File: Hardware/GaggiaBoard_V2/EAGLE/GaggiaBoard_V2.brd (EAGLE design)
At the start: 102 x 92 mm, 115 parts, among them IC1 LD117AS33TR, J1 4PIN, J11 PIN262409-1, J12 PIN262409-1, J13 PIN262409-1, J14 PIN262409-1, J15 PIN262409-1, J16 PIN262409-1, J17 PIN262409-1, J18 PIN262409-1, J19 PIN262409-1, J2 Vertical Qwiic Connector, J20 PIN262409-1, J3 Vertical Qwiic Connector, J5 2PIN, J6 3PIN, J7 3PIN, J8 5PIN, J9 3PIN, K1 RELAY-SPDT-JZC-11F, K2 RELAY-SPDT-JZC-11F, K3 AQH213, Q1 600mA/40V, Q10 600mA/40V, Q2 600mA/40V, Q3 600mA/40V, Q4 600mA/40V, Q5 600mA/40V, Q6 600mA/40V, Q8 600mA/40V, Q9 600mA/40V, U1 BLACKPILL, U2 MAX31855K, U5 TXS0102

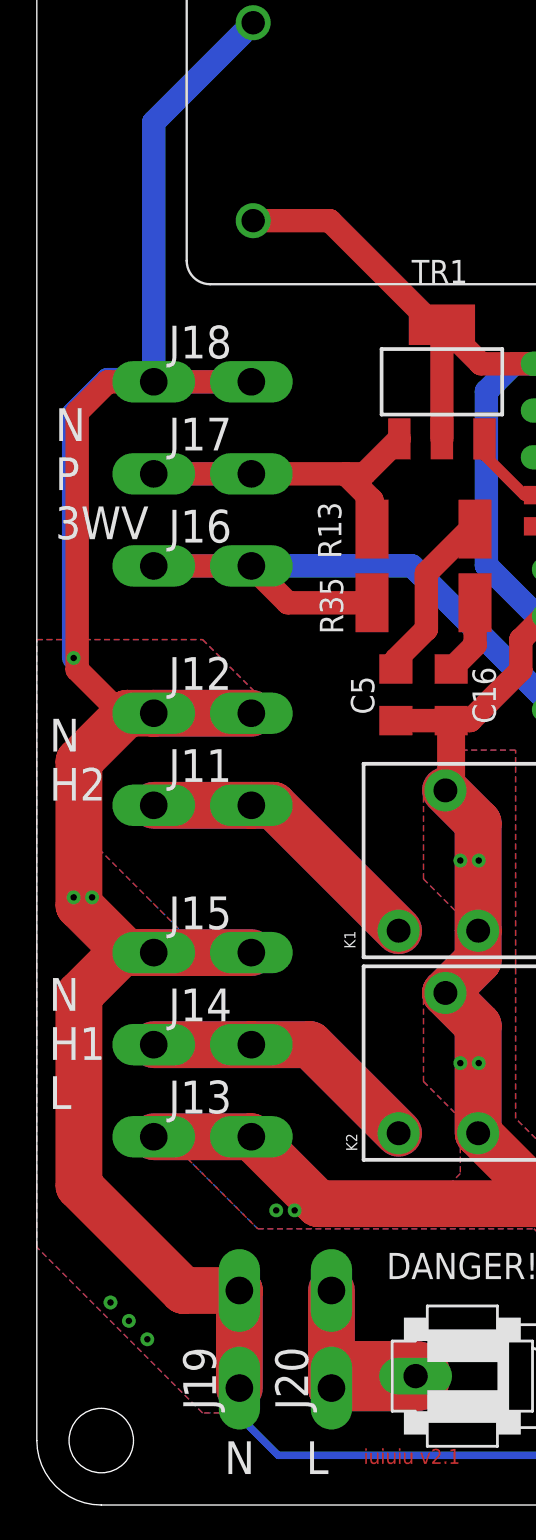
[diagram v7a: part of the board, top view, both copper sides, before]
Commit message: Faston drill fix
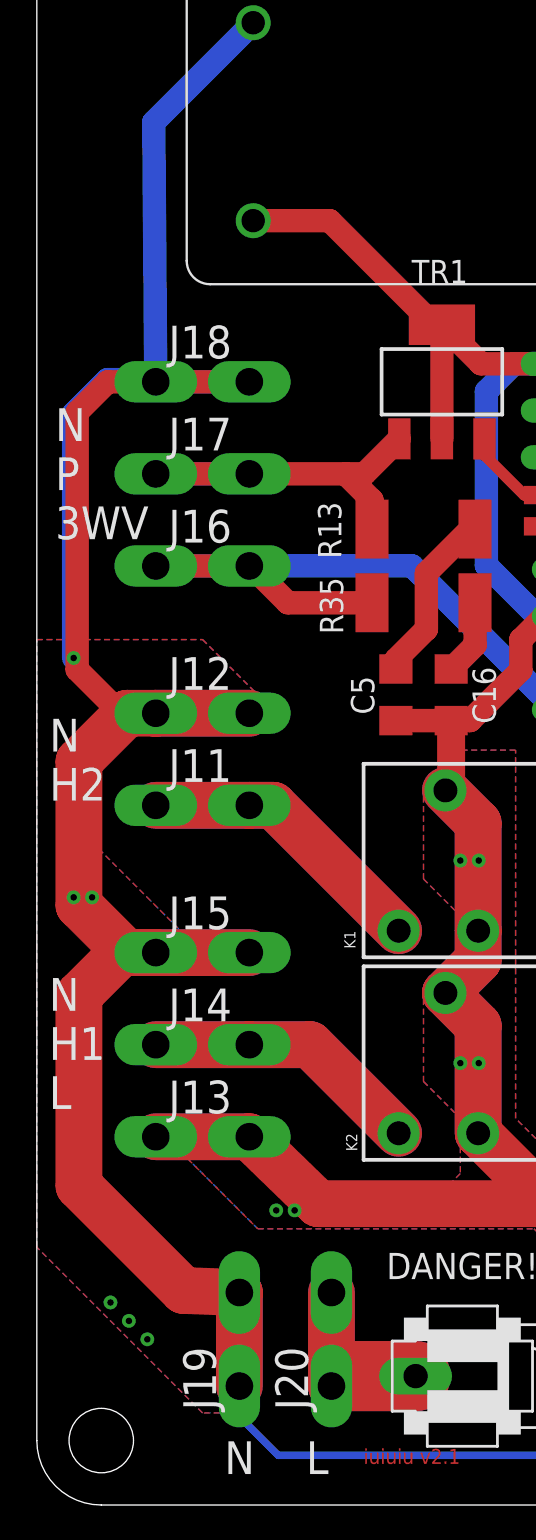
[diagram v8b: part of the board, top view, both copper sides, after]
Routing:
- net AC_N: track 200.9 -> 199.9 mm
- net N$1: track 20.3 -> 19.7 mm
